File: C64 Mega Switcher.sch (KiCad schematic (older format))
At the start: 25 parts, among them J1 Port 1, J2 Port 2, J3 Mega Drive, J4 C_SEL, J5 B_SEL, SW1 P1_SEL, SW2 P2_SEL, U1 74HCT4053, U2 74HCT4053, U3 NE555

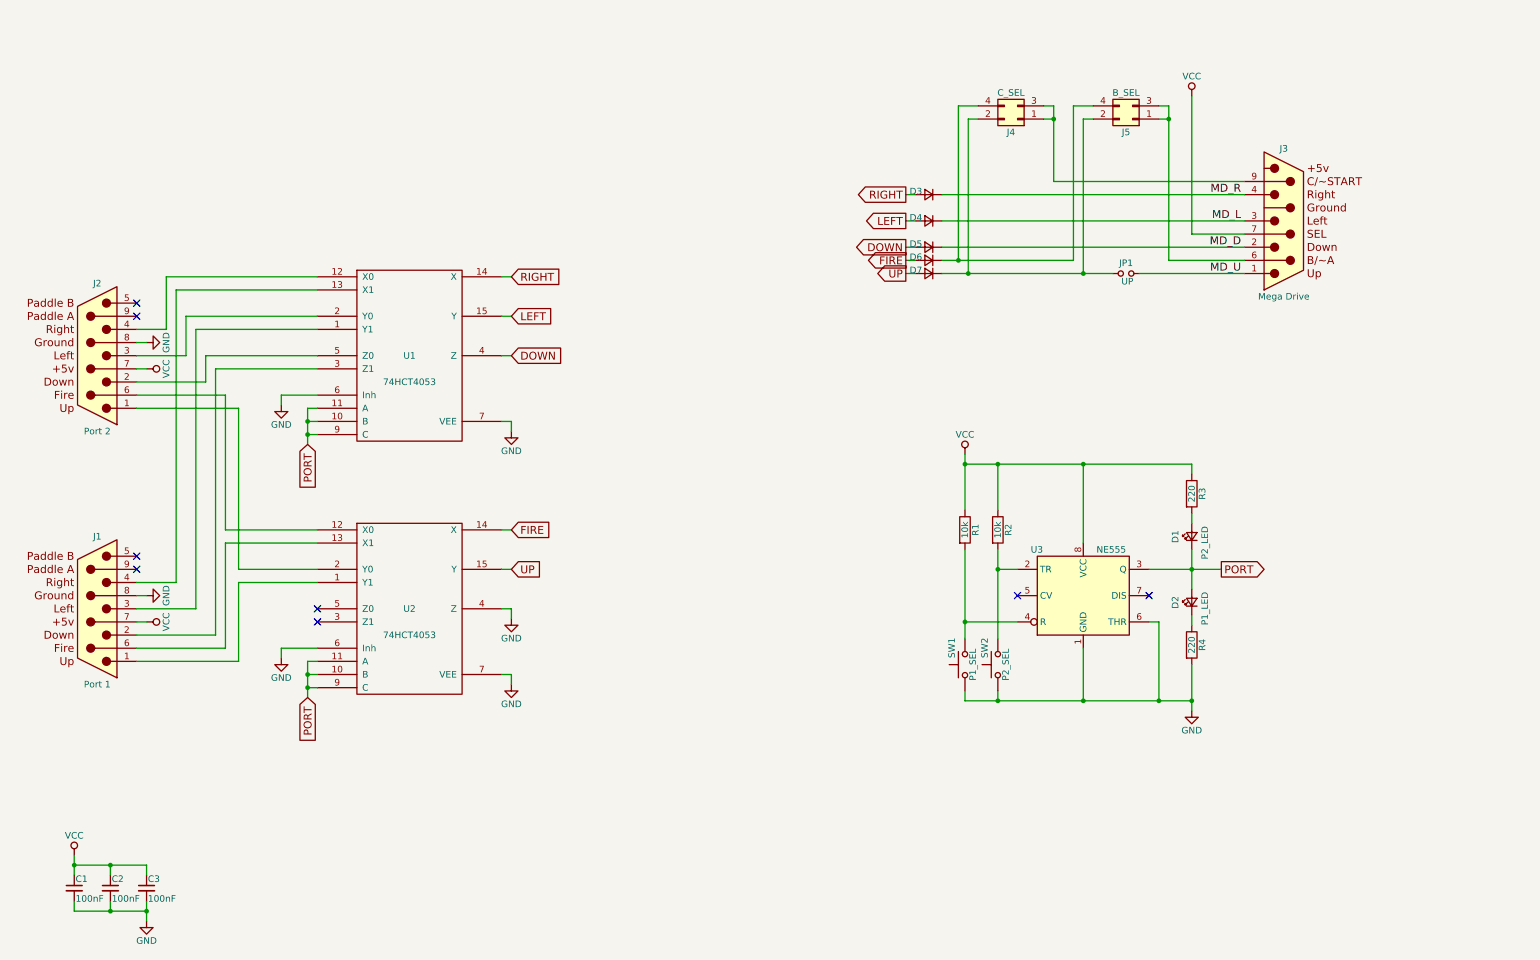
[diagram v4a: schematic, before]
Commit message: Added silkscreen warnings
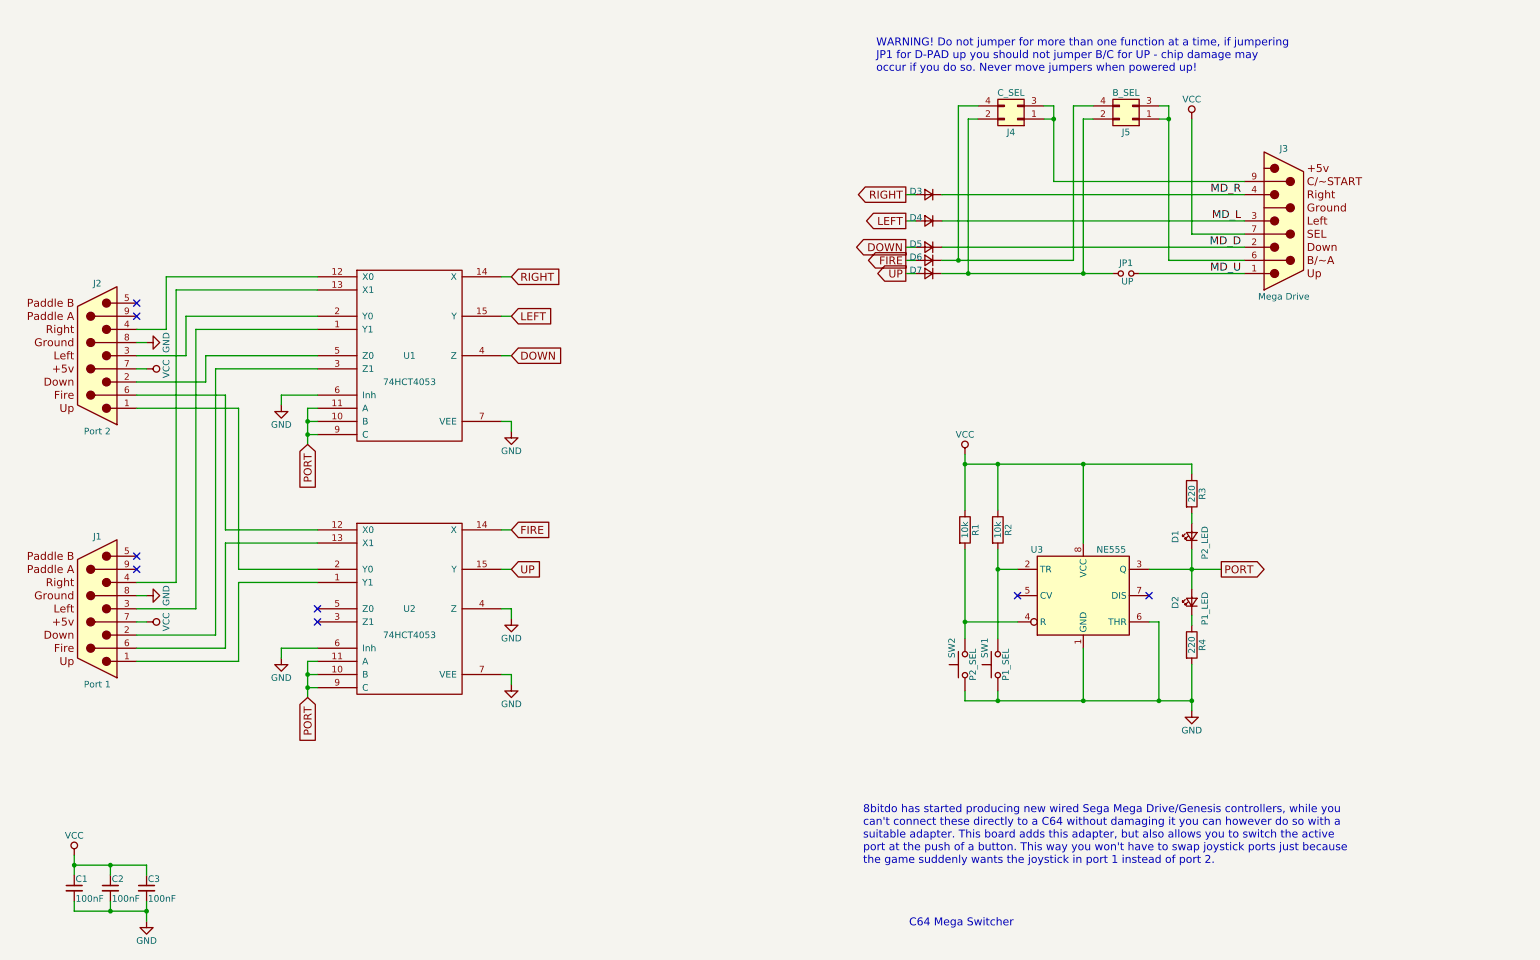
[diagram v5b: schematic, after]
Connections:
- net at R2.2, U3.2 (TR): now also SW1.2; no longer SW2.2
- net at R1.2, U3.4 (R): now also SW2.2; no longer SW1.2
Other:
- note added: "8bitdo has started producing new wired Sega Mega Drive/Genesis controllers, while you\ncan't connect these directly to a C64 without damaging it you can however do so with a\nsuitable adapter. This board adds this adapter, but also allows you to switch the active\nport at the push of a button. This way you won't have to swap joystick ports just because\nthe game suddenly wants the joystick in por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"
- note added: "C64 Mega Switcher"
- note added: "WARNING! Do not jumper for more than one function at a time, if jumpering \nJP1 for D-PAD up you should not jumper B/C for UP - chip damage may\noccur if you do so. Never move jumpers when powered up!"
- moved on the sheet: SW1, SW2
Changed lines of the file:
@@
 L SW_Push SW1
 U 1 1 5D1420E9
+P 8025 5500
+F 0 "SW1" H 8075 5600 50  0000 L CNN
+F 1 "P1_SEL" H 8025 5440 50  0000 C CNN
+F 2 "Buttons_Switches_THT:SW_PUSH_6mm" H 8025 5700 50  0001 C CNN
+F 3 "" H 8025 5700 50  0001 C CNN
+	1    8025 5500
+	0    -1   -1   0
+$EndComp
+$Comp
+L SW_Push SW2
+U 1 1 5D1424D3
 P 7775 5500
-F 0 "SW1" H 7825 5600 50  0000 L CNN
-F 1 "P1_SEL" H 7775 5440 50  0000 C CNN
+F 0 "SW2" H 7825 5600 50  0000 L CNN
+F 1 "P2_SEL" H 7775 5440 50  0000 C CNN
 F 2 "Buttons_Switches_THT:SW_PUSH_6mm" H 7775 5700 50  0001 C CNN
 F 3 "" H 7775 5700 50  0001 C CNN
 	1    7775 5500
-	0    -1   -1   0
-$EndComp
-$Comp
-L SW_Push SW2
-U 1 1 5D1424D3
-P 8025 5500
-F 0 "SW2" H 8075 5600 50  0000 L CNN
-F 1 "P2_SEL" H 8025 5440 50  0000 C CNN
-F 2 "Buttons_Switches_THT:SW_PUSH_6mm" H 8025 5700 50  0001 C CNN
-F 3 "" H 8025 5700 50  0001 C CNN
-	1    8025 5500
 	0    -1   -1   0
 $EndComp
@@
 	8750 1250 8600 1250
 Wire Wire Line
-	8600 1250 8600 2425
-Wire Wire Line
-	8600 2425 7600 2425
+	8600 2425 8600 1250
+Wire Wire Line
+	7600 2425 8600 2425
 Wire Wire Line
 	8450 1250 8450 1825
@@
 Wire Wire Line
 	8375 1250 8450 1250
-Wire Wire Line
-	9500 1175 9500 2225
 Wire Wire Line
 	9500 2225 9900 2225
@@
 	9175 5175 9250 5175
 Wire Wire Line
-	9250 5175 9250 5775
+	9250 5775 9250 5175
 Wire Wire Line
 	7775 5700 7775 5775
@@
 L VCC #PWR010
 U 1 1 5D11DA0F
-P 9500 1175
-F 0 "#PWR010" H 9500 1025 50  0001 C CNN
-F 1 "VCC" H 9500 1325 50  0000 C CNN
-F 2 "" H 9500 1175 50  0001 C CNN
-F 3 "" H 9500 1175 50  0001 C CNN
-	1    9500 1175
+P 9500 1350
+F 0 "#PWR010" H 9500 1200 50  0001 C CNN
+F 1 "VCC" H 9500 1500 50  0000 C CNN
+F 2 "" H 9500 1350 50  0001 C CNN
+F 3 "" H 9500 1350 50  0001 C CNN
+	1    9500 1350
 	1    0    0    -1
 $EndComp
@@
 Wire Wire Line
 	7400 2525 7325 2525
+Text Notes 7350 7500 0    60   ~ 0
+C64 Mega Switcher
+Text Notes 7000 7025 0    60   ~ 0
+8bitdo has started producing new wired Sega Mega Drive/Genesis controllers, while you\ncan't connect these directly to a C64 without damaging it you can however do so with a\nsuitable adapter. This board adds this adapter, but also allows you to switch the active\nport at the push of a button. This way you won't have to swap joystick ports just because\nthe game suddenly wants the joystick in port 1 instead of port 2.
+Text Notes 7100 1000 0    60   ~ 0
+WARNING! Do not jumper for more than one function at a time, if jumpering \nJP1 for D-PAD up you should not jumper B/C for UP - chip damage may\noccur if you do so. Never move jumpers when powered up!
+Wire Wire Line
+	9500 1350 9500 2225
 $EndSCHEMATC

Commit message: Updated PCB with ALT-FIRE, assigned new footprints
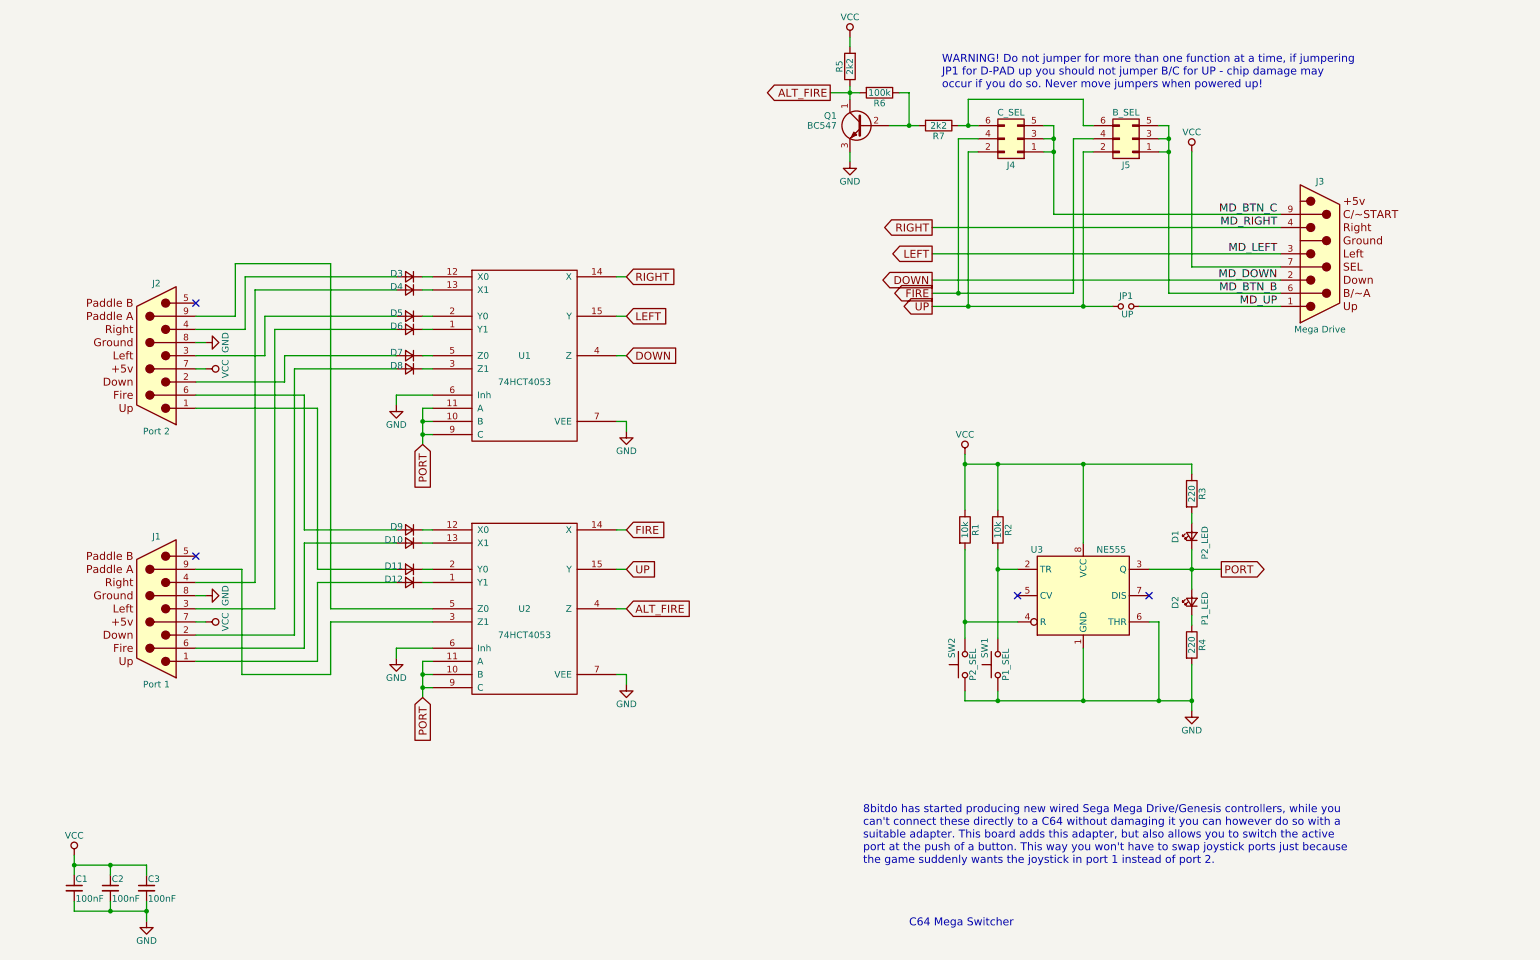
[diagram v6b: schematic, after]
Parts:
- removed J4: C_SEL, Pin_Headers:Pin_Header_Straight_2x02_Pitch2.54mm, symbol Conn_02x02_Odd_Even
- removed J5: B_SEL, Pin_Headers:Pin_Header_Straight_2x02_Pitch2.54mm, symbol Conn_02x02_Odd_Even
- added D10, D11, D12, D8, D9: 1N4148, Diodes_THT:D_DO-35_SOD27_P2.54mm_Vertical_AnodeUp, symbol D_Small
- added J4: C_SEL, Pin_Headers:Pin_Header_Angled_2x03_Pitch2.54mm, symbol Conn_02x03_Odd_Even
- added J5: B_SEL, Pin_Headers:Pin_Header_Angled_2x03_Pitch2.54mm, symbol Conn_02x03_Odd_Even
- added Q1: BC547, TO_SOT_Packages_THT:TO-92_Molded_Narrow, symbol BC547
- added R5, R7: 2k2, Resistors_THT:R_Axial_DIN0207_L6.3mm_D2.5mm_P10.16mm_Horizontal, symbol R
- added R6: 100k, Resistors_THT:R_Axial_DIN0207_L6.3mm_D2.5mm_P10.16mm_Horizontal, symbol R
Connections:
- net DOWN: now also J3.2; no longer D5.2 (A)
- net FIRE: now also J4.4 (Pin_4), J5.4 (Pin_4); no longer D6.2 (A)
- net GND: now also Q1.3 (E); no longer U2.4 (Z)
- net LEFT: now also J3.3; no longer D4.2 (A)
- net RIGHT: now also J3.4; no longer D3.2 (A)
- net UP: now also JP1.1, J4.2 (Pin_2), J5.2 (Pin_2); no longer D7.2 (A)
- net VCC: now also R5.2
- net at U1.1 (Y1): now also D6.1 (K); no longer J1.3
- net at U1.12 (X0): now also D3.1 (K); no longer J2.4
- net at U1.13 (X1): now also D4.1 (K); no longer J1.4
- net at U1.2 (Y0): now also D5.1 (K); no longer J2.3
- net at U1.3 (Z1): now also D8.1 (K); no longer J1.2
- net at U1.5 (Z0): now also D7.1 (K); no longer J2.2
- net at U2.1 (Y1): now also D12.1 (K); no longer J1.1
- net at U2.12 (X0): now also D9.1 (K); no longer J2.6
- net at U2.13 (X1): now also D10.1 (K); no longer J1.6
- net at U2.2 (Y0): now also D11.1 (K); no longer J2.1
- net at U2.3 (Z1): now also J1.9
- net at U2.5 (Z0): now also J2.9
- net MD_BTN_B: now reaches J3.6
- net MD_BTN_B: now also J5.1 (Pin_1), J5.3 (Pin_3), J5.5 (Pin_5)
- net MD_BTN_C: now reaches J3.9
- net MD_BTN_C: now also J4.1 (Pin_1), J4.3 (Pin_3), J4.5 (Pin_5)
- removed net MD_D: D5.1 (K), J3.2
- removed net MD_L: D4.1 (K), J3.3
- removed net MD_R: D3.1 (K), J3.4
- net MD_U renamed MD_UP
- new net: D11.2 (A), J2.1
- new net: D7.2 (A), J2.2
- new net: D5.2 (A), J2.3
- new net: D3.2 (A), J2.4
- new net: D9.2 (A), J2.6
- new net: D12.2 (A), J1.1
- new net: D8.2 (A), J1.2
- new net: D6.2 (A), J1.3
- new net: D4.2 (A), J1.4
- new net: D10.2 (A), J1.6
- new net: J4.6 (Pin_6), J5.6 (Pin_6), R7.1
- new net: Q1.2 (B), R6.1, R7.2
- new net ALT_FIRE: Q1.1 (C), R5.1, R6.2, U2.4 (Z)
- no-connect marks 8 -> 4
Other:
- moved on the sheet: D3, D4, D5, D6, D7, J1, J2, J3, JP1, U1, U2

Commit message: Revision B
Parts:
- J4, J5: footprint Pin_Headers:Pin_Header_Angled_2x03_Pitch2.54mm -> Pin_Headers:Pin_Header_Straight_2x03_Pitch2.54mm
- Q1: footprint TO_SOT_Packages_THT:TO-92_Molded_Narrow -> TO_SOT_Packages_THT:TO-92_Inline_Wide
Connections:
- net ALT_FIRE: now also R6.1; no longer R6.2
- net GND: now also R4.1; no longer R4.2
- net VCC: now also R1.2, R2.2, R3.2; no longer R1.1, R2.1, R3.1
- net at SW1.2, U3.2 (TR): now also R2.1; no longer R2.2
- net at SW2.2, U3.4 (R): now also R1.1; no longer R1.2
- net at D2.1 (K): now also R4.2; no longer R4.1
- net at D1.2 (A): now also R3.1; no longer R3.2
- net at Q1.2 (B), R7.2: now also R6.2; no longer R6.1
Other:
- note added: "B"
- note added: "WARNING! Do not jumper for more than one function at a time, if jumpering \nJP1 for D-PAD up - then you should not jumper B or C for UP, in short \nno overlap vertically or horizontally. Never move jumpers when powered up!"
- note removed: "WARNING! Do not jumper for more than one function at a time, if jumpering \nJP1 for D-PAD up you should not jumper B/C for UP - chip damage may\noccur if you do so. Never move jumpers when powered up!"
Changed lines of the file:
@@
 F 3 "" H 8025 4475 50  0001 C CNN
 	1    8025 4475
-	1    0    0    -1
+	-1   0    0    1
 $EndComp
 $Comp
@@
 F 3 "" H 7775 4475 50  0001 C CNN
 	1    7775 4475
-	1    0    0    -1
+	-1   0    0    1
 $EndComp
 NoConn ~ 8175 4975
@@
 F 3 "" H 9500 5350 50  0001 C CNN
 	1    9500 5350
-	1    0    0    -1
+	-1   0    0    1
 $EndComp
 $Comp
@@
 F 3 "" H 9500 4200 50  0001 C CNN
 	1    9500 4200
-	1    0    0    -1
+	-1   0    0    1
 $EndComp
 $Comp
@@
 $EndComp
 $Comp
-L VCC #PWR1
+L VCC #PWR01
 U 1 1 5D11C338
 P 1000 6950
-F 0 "#PWR1" H 1000 6800 50  0001 C CNN
+F 0 "#PWR01" H 1000 6800 50  0001 C CNN
 F 1 "VCC" H 1000 7100 50  0000 C CNN
 F 2 "" H 1000 6950 50  0001 C CNN
@@
 $EndComp
 $Comp
-L GND #PWR2
+L GND #PWR02
 U 1 1 5D11C374
 P 1550 7450
-F 0 "#PWR2" H 1550 7200 50  0001 C CNN
+F 0 "#PWR02" H 1550 7200 50  0001 C CNN
 F 1 "GND" H 1550 7300 50  0000 C CNN
 F 2 "" H 1550 7450 50  0001 C CNN
@@
 $EndComp
 $Comp
-L GND #PWR8
+L GND #PWR03
 U 1 1 5D11CABA
 P 3450 5450
-F 0 "#PWR8" H 3450 5200 50  0001 C CNN
+F 0 "#PWR03" H 3450 5200 50  0001 C CNN
 F 1 "GND" H 3450 5300 50  0000 C CNN
 F 2 "" H 3450 5450 50  0001 C CNN
@@
 $EndComp
 $Comp
-L GND #PWR10
+L GND #PWR04
 U 1 1 5D11CB08
 P 5200 5650
-F 0 "#PWR10" H 5200 5400 50  0001 C CNN
+F 0 "#PWR04" H 5200 5400 50  0001 C CNN
 F 1 "GND" H 5200 5500 50  0000 C CNN
 F 2 "" H 5200 5650 50  0001 C CNN
@@
 $EndComp
 $Comp
-L GND #PWR7
+L GND #PWR05
 U 1 1 5D11D0E1
 P 3450 3525
-F 0 "#PWR7" H 3450 3275 50  0001 C CNN
+F 0 "#PWR05" H 3450 3275 50  0001 C CNN
 F 1 "GND" H 3450 3375 50  0000 C CNN
 F 2 "" H 3450 3525 50  0001 C CNN
@@
 $EndComp
 $Comp
-L GND #PWR9
+L GND #PWR06
 U 1 1 5D11D128
 P 5200 3725
-F 0 "#PWR9" H 5200 3475 50  0001 C CNN
+F 0 "#PWR06" H 5200 3475 50  0001 C CNN
 F 1 "GND" H 5200 3575 50  0000 C CNN
 F 2 "" H 5200 3725 50  0001 C CNN
@@
 $EndComp
 $Comp
-L GND #PWR15
+L GND #PWR07
 U 1 1 5D11D237
 P 9500 5850
-F 0 "#PWR15" H 9500 5600 50  0001 C CNN
+F 0 "#PWR07" H 9500 5600 50  0001 C CNN
 F 1 "GND" H 9500 5700 50  0000 C CNN
 F 2 "" H 9500 5850 50  0001 C CNN
@@
 $EndComp
 $Comp
-L VCC #PWR13
+L VCC #PWR08
 U 1 1 5D11D810
 P 7775 3900
-F 0 "#PWR13" H 7775 3750 50  0001 C CNN
+F 0 "#PWR08" H 7775 3750 50  0001 C CNN
 F 1 "VCC" H 7775 4050 50  0000 C CNN
 F 2 "" H 7775 3900 50  0001 C CNN
@@
 $EndComp
 $Comp
-L VCC #PWR14
+L VCC #PWR09
 U 1 1 5D11DA0F
 P 9500 1600
-F 0 "#PWR14" H 9500 1450 50  0001 C CNN
+F 0 "#PWR09" H 9500 1450 50  0001 C CNN
 F 1 "VCC" H 9500 1750 50  0000 C CNN
 F 2 "" H 9500 1600 50  0001 C CNN
@@
 $EndComp
 $Comp
-L GND #PWR3
+L GND #PWR010
 U 1 1 5D11F688
 P 2000 3050
-F 0 "#PWR3" H 2000 2800 50  0001 C CNN
+F 0 "#PWR010" H 2000 2800 50  0001 C CNN
 F 1 "GND" H 2000 2900 50  0000 C CNN
 F 2 "" H 2000 3050 50  0001 C CNN
@@
 $EndComp
 $Comp
-L VCC #PWR4
+L VCC #PWR011
 U 1 1 5D11F85F
 P 2000 3250
-F 0 "#PWR4" H 2000 3100 50  0001 C CNN
+F 0 "#PWR011" H 2000 3100 50  0001 C CNN
 F 1 "VCC" H 2000 3400 50  0000 C CNN
 F 2 "" H 2000 3250 50  0001 C CNN
@@
 $EndComp
 $Comp
-L VCC #PWR6
+L VCC #PWR012
 U 1 1 5D11FDDD
 P 2000 5175
-F 0 "#PWR6" H 2000 5025 50  0001 C CNN
+F 0 "#PWR012" H 2000 5025 50  0001 C CNN
 F 1 "VCC" H 2000 5325 50  0000 C CNN
 F 2 "" H 2000 5175 50  0001 C CNN
@@
 $EndComp
 $Comp
-L GND #PWR5
+L GND #PWR013
 U 1 1 5D120002
 P 2000 4975
-F 0 "#PWR5" H 2000 4725 50  0001 C CNN
+F 0 "#PWR013" H 2000 4725 50  0001 C CNN
 F 1 "GND" H 2000 4825 50  0000 C CNN
 F 2 "" H 2000 4975 50  0001 C CNN
@@
 Text Notes 7000 7025 0    60   ~ 0
 8bitdo has started producing new wired Sega Mega Drive/Genesis controllers, while you\ncan't connect these directly to a C64 without damaging it you can however do so with a\nsuitable adapter. This board adds this adapter, but also allows you to switch the active\nport at the push of a button. This way you won't have to swap joystick ports just because\nthe game suddenly wants the joystick in port 1 instead of port 2.
-Text Notes 7600 1125 0    60   ~ 0
-WARNING! Do not jumper for more than one function at a time, if jumpering \nJP1 for D-PAD up you should not jumper B/C for UP - chip damage may\noccur if you do so. Never move jumpers when powered up!
+Text Notes 7500 1150 0    60   ~ 0
+WARNING! Do not jumper for more than one function at a time, if jumpering \nJP1 for D-PAD up - then you should not jumper B or C for UP, in short \nno overlap vertically or horizontally. Never move jumpers when powered up!
 $Comp
 L D_Small D8
@@
 F 0 "J4" H 8225 1700 50  0000 C CNN
 F 1 "C_SEL" H 8225 1300 50  0000 C CNN
-F 2 "Pin_Headers:Pin_Header_Angled_2x03_Pitch2.54mm" H 8175 1500 50  0001 C CNN
+F 2 "Pin_Headers:Pin_Header_Straight_2x03_Pitch2.54mm" H 8175 1500 50  0001 C CNN
 F 3 "" H 8175 1500 50  0001 C CNN
 	1    8175 1500
@@
 F 0 "J5" H 9100 1700 50  0000 C CNN
 F 1 "B_SEL" H 9100 1300 50  0000 C CNN
-F 2 "Pin_Headers:Pin_Header_Angled_2x03_Pitch2.54mm" H 9050 1500 50  0001 C CNN
+F 2 "Pin_Headers:Pin_Header_Straight_2x03_Pitch2.54mm" H 9050 1500 50  0001 C CNN
 F 3 "" H 9050 1500 50  0001 C CNN
 	1    9050 1500
@@
 F 0 "Q1" H 7200 1475 50  0000 L CNN
 F 1 "BC547" H 7200 1400 50  0000 L CNN
-F 2 "TO_SOT_Packages_THT:TO-92_Molded_Narrow" H 7200 1325 50  0001 L CIN
+F 2 "TO_SOT_Packages_THT:TO-92_Inline_Wide" H 7200 1325 50  0001 L CIN
 F 3 "" H 7000 1400 50  0001 L CNN
 	1    7000 1400
@@
 F 3 "" H 7125 1150 50  0001 C CNN
 	1    7125 1150
-	0    1    1    0
+	0    -1   -1   0
 $EndComp
 Wire Wire Line
@@
 Connection ~ 6900 1150
 $Comp
-L VCC #PWR11
+L VCC #PWR014
 U 1 1 5D736FCC
 P 6900 725
-F 0 "#PWR11" H 6900 575 50  0001 C CNN
+F 0 "#PWR014" H 6900 575 50  0001 C CNN
 F 1 "VCC" H 6900 875 50  0000 C CNN
 F 2 "" H 6900 725 50  0001 C CNN
@@
 ALT_FIRE
 $Comp
-L GND #PWR12
+L GND #PWR015
 U 1 1 5D737AC0
 P 6900 1675
-F 0 "#PWR12" H 6900 1425 50  0001 C CNN
+F 0 "#PWR015" H 6900 1425 50  0001 C CNN
 F 1 "GND" H 6900 1525 50  0000 C CNN
 F 2 "" H 6900 1675 50  0001 C CNN
@@
 Wire Wire Line
 	6900 1600 6900 1675
+Text Notes 10550 7650 0    60   ~ 0
+B
 $EndSCHEMATC
